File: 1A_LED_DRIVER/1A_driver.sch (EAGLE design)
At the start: 1 part

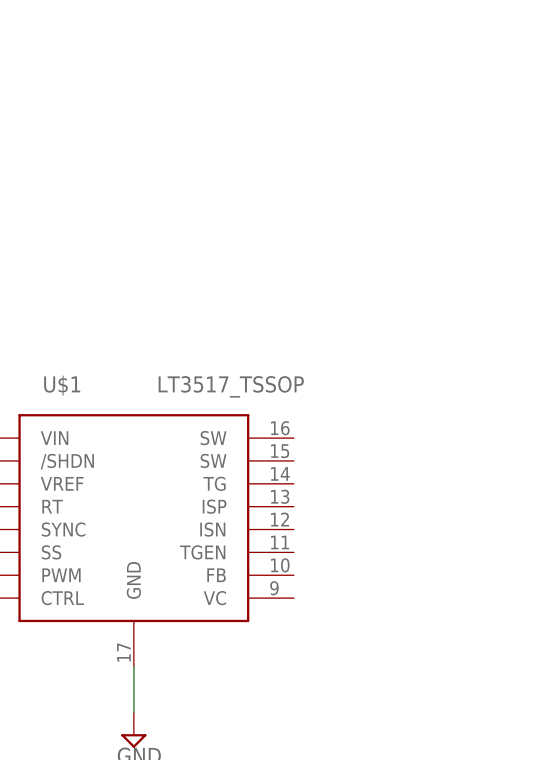
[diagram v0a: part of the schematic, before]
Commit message: making new mosfet lib
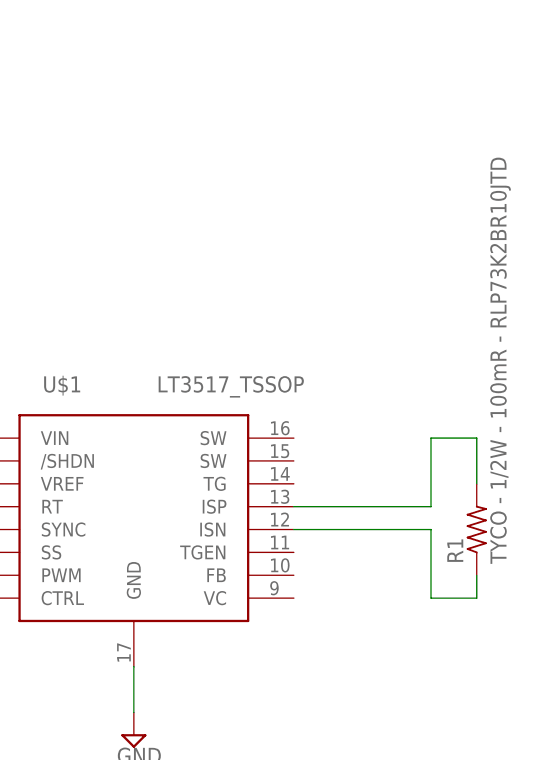
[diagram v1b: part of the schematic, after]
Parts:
- added R1: TYCO - 1/2W - 100mR - RLP73K2BR10JTD, standard_passive:RES_1206
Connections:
- new net N$1: R1.2, U$1.ISP@13
- new net N$2: R1.1, U$1.ISN@12
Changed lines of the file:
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@@
 <setting verticaltext="up"/>
 </settings>
-<grid distance="0.1" unitdist="inch" unit="inch" style="lines" multiple="1" display="yes" altdistance="0.01" altunitdist="inch" altunit="inch"/>
+<grid distance="0.1" unitdist="inch" unit="mm" style="lines" multiple="1" display="yes" altdistance="0.01" altunitdist="inch" altunit="mm"/>
 <layers>
 <layer number="1" name="Top" color="4" fill="1" visible="no" active="no"/>
@@
 <part name="U$1" library="LT3517" deviceset="LT3517_TSSOP" device=""/>
 <part name="SUPPLY1" library="supply2" deviceset="GND" device=""/>
+<part name="R1" library="standard_passive" deviceset="RES_1206" device="" value="TYCO - 1/2W - 100mR - RLP73K2BR10JTD"/>
 </parts>
 <sheets>
@@
 <instance part="U$1" gate="G$1" x="195.58" y="129.54"/>
 <instance part="SUPPLY1" gate="GND" x="195.58" y="104.14"/>
+<instance part="R1" gate="G$1" x="233.68" y="127" rot="R90"/>
 </instances>
 <busses>
@@
 </segment>
 </net>
+<net name="N$1" class="0">
+<segment>
+<pinref part="U$1" gate="G$1" pin="ISP@13"/>
+<wire x1="213.36" y1="129.54" x2="228.6" y2="129.54" width="0.1524" layer="91"/>
+<wire x1="228.6" y1="129.54" x2="228.6" y2="137.16" width="0.1524" layer="91"/>
+<wire x1="228.6" y1="137.16" x2="233.68" y2="137.16" width="0.1524" layer="91"/>
+<pinref part="R1" gate="G$1" pin="2"/>
+<wire x1="233.68" y1="137.16" x2="233.68" y2="132.08" width="0.1524" layer="91"/>
+</segment>
+</net>
+<net name="N$2" class="0">
+<segment>
+<pinref part="U$1" gate="G$1" pin="ISN@12"/>
+<wire x1="213.36" y1="127" x2="228.6" y2="127" width="0.1524" layer="91"/>
+<wire x1="228.6" y1="127" x2="228.6" y2="119.38" width="0.1524" layer="91"/>
+<wire x1="228.6" y1="119.38" x2="233.68" y2="119.38" width="0.1524" layer="91"/>
+<pinref part="R1" gate="G$1" pin="1"/>
+<wire x1="233.68" y1="119.38" x2="233.68" y2="121.92" width="0.1524" layer="91"/>
+</segment>
+</net>

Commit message: schematic finished
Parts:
- added C1, C2: 0.1u, standard_passive:CAP_0603
- added C3: 4.7u, standard_passive:CAP_1206
- added C4: 0.22u, standard_passive:CAP_0603
- added D1: RB060MM-60TF, DIODES:SCH_DIODE
- added L1: 6.8u, WE-PD:WE-PD-744771006_1260/1245/1280/1210
- added Q1: ZXMP6A13FTA, MOSFET:P-CHAN_MOSFET
- added R2, R3, R4, R5: (no value), standard_passive:RES_0603
- added R6: 6.04k, standard_passive:RES_0603
- added SV1: (no value), con-lstb:MA04-1
- added X1: 22-23-2021, con-molex:22-23-2021
- R1: value TYCO - 1/2W - 100mR - RLP73K2BR10JTD -> 100mR - 1/2W
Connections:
- new net N$10: C1.1, U$1.VC@9
- new net N$11: R6.1, U$1.RT@4
- new net N$3: Q1.G, U$1.TG@14
- new net N$4: D1.A, L1.2, U$1.SW@15, U$1.SW@16
- new net N$5: Q1.D, X1-1.S
- new net N$6: R2.1, R3.2, U$1.FB@10
- new net N$8: C2.2, U$1.SS@6
- new net N$9: R4.2, R5.1, U$1.CTRL@8
- new net PWM: SV1.3, U$1.PWM@7
- new net VIN: C3.1, L1.1, SV1.4, U$1./SHDN@2, U$1.VIN@1, X1-2.S
- new net VREF: R4.1, U$1.TGEN@11, U$1.VREF@3
- net GND: now also C1.2, C2.1, C4.2, R3.1, R5.2, R6.2, SV1.1, SV1.2, U$1.SYNC@5
- net N$1: now also C3.2, C4.1, D1.C, R2.2
- net N$2: now also Q1.S
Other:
- note added: "Only R4 if CTRL is not used"
- moved on the sheet: R1

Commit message: need to finish layout for the 1A regulator
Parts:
- added C5: 4.7u, standard_passive:CAP_1206
- added C7: 100u, rcl:CPOL-EUE5-5
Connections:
- net N$1 renamed I_P
- net N$2 renamed I_N
- net N$5 renamed I_LED
- net GND: now also C5.1, C7.-
- net VIN: now also C5.2, C7.+
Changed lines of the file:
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@@
 <setting verticaltext="up"/>
 </settings>
-<grid distance="0.1" unitdist="inch" unit="inch" style="lines" multiple="1" display="yes" altdistance="0.01" altunitdist="inch" altunit="inch"/>
+<grid distance="0.1" unitdist="inch" unit="mm" style="lines" multiple="1" display="yes" altdistance="0.01" altunitdist="inch" altunit="mm"/>
 <layers>
 <layer number="1" name="Top" color="4" fill="1" visible="no" active="no"/>
@@
 <part name="SV1" library="con-lstb" deviceset="MA04-1" device=""/>
 <part name="SUPPLY7" library="supply2" deviceset="GND" device=""/>
+<part name="C5" library="standard_passive" deviceset="CAP_1206" device="" value="4.7u"/>
+<part name="SUPPLY8" library="supply2" deviceset="GND" device=""/>
+<part name="C7" library="rcl" deviceset="CPOL-EU" device="E5-5" value="100u"/>
+<part name="SUPPLY9" library="supply2" deviceset="GND" device=""/>
 </parts>
 <sheets>
@@
 <instance part="SV1" gate="1" x="129.54" y="165.1"/>
 <instance part="SUPPLY7" gate="GND" x="142.24" y="152.4"/>
+<instance part="C5" gate="G$1" x="160.02" y="160.02" rot="R180"/>
+<instance part="SUPPLY8" gate="GND" x="160.02" y="152.4"/>
+<instance part="C7" gate="G$1" x="165.1" y="162.56"/>
+<instance part="SUPPLY9" gate="GND" x="165.1" y="152.4"/>
 </instances>
 <busses>
@@
 <junction x="142.24" y="160.02"/>
 </segment>
-</net>
-<net name="N$1" class="0">
+<segment>
+<pinref part="C5" gate="G$1" pin="1"/>
+<pinref part="SUPPLY8" gate="GND" pin="GND"/>
+<wire x1="160.02" y1="157.48" x2="160.02" y2="154.94" width="0.1524" layer="91"/>
+</segment>
+<segment>
+<pinref part="C7" gate="G$1" pin="-"/>
+<pinref part="SUPPLY9" gate="GND" pin="GND"/>
+<wire x1="165.1" y1="157.48" x2="165.1" y2="154.94" width="0.1524" layer="91"/>
+</segment>
+</net>
+<net name="I_P" class="0">
 <segment>
 <pinref part="U$1" gate="G$1" pin="ISP@13"/>
@@
 <wire x1="266.7" y1="160.02" x2="259.08" y2="160.02" width="0.1524" layer="91"/>
 <junction x="259.08" y="160.02"/>
-</segment>
-</net>
-<net name="N$2" class="0">
+<label x="223.52" y="129.54" size="1.778" layer="95"/>
+</segment>
+</net>
+<net name="I_N" class="0">
 <segment>
 <pinref part="U$1" gate="G$1" pin="ISN@12"/>
@@
 <wire x1="259.08" y1="119.38" x2="259.08" y2="114.3" width="0.1524" layer="91"/>
 <junction x="259.08" y="119.38"/>
+<label x="223.52" y="127" size="1.778" layer="95"/>
 </segment>
 </net>
@@
 </segment>
 </net>
-<net name="N$5" class="0">
+<net name="I_LED" class="0">
 <segment>
 <pinref part="Q1" gate="G$1" pin="D"/>
@@
 <pinref part="X1" gate="-1" pin="S"/>
 <wire x1="259.08" y1="99.06" x2="266.7" y2="99.06" width="0.1524" layer="91"/>
+<label x="261.62" y="99.06" size="1.778" layer="95"/>
 </segment>
 </net>
@@
 </net>
 <net name="VIN" class="0">
+<segment>
+<pinref part="X1" gate="-2" pin="S"/>
+<wire x1="266.7" y1="96.52" x2="248.92" y2="96.52" width="0.1524" layer="91"/>
+<label x="251.46" y="96.52" size="1.778" layer="95"/>
+</segment>
 <segment>
 <pinref part="L1" gate="G$1" pin="1"/>
@@
 <pinref part="C3" gate="G$1" pin="1"/>
 <wire x1="203.2" y1="160.02" x2="228.6" y2="160.02" width="0.1524" layer="91"/>
-</segment>
-<segment>
-<pinref part="X1" gate="-2" pin="S"/>
-<wire x1="266.7" y1="96.52" x2="248.92" y2="96.52" width="0.1524" layer="91"/>
-<label x="251.46" y="96.52" size="1.778" layer="95"/>
-</segment>
-<segment>
+<wire x1="172.72" y1="167.64" x2="172.72" y2="149.86" width="0.1524" layer="91"/>
+<junction x="172.72" y="149.86"/>
 <pinref part="SV1" gate="1" pin="4"/>
-<wire x1="137.16" y1="167.64" x2="149.86" y2="167.64" width="0.1524" layer="91"/>
-<label x="142.24" y="167.64" size="1.778" layer="95"/>
-</segment>
-</net>
+<wire x1="137.16" y1="167.64" x2="160.02" y2="167.64" width="0.1524" layer="91"/>
+<pinref part="C5" gate="G$1" pin="2"/>
+<wire x1="160.02" y1="167.64" x2="165.1" y2="167.64" width="0.1524" layer="91"/>
+<wire x1="165.1" y1="167.64" x2="172.72" y2="167.64" width="0.1524" layer="91"/>
+<wire x1="160.02" y1="165.1" x2="160.02" y2="167.64" width="0.1524" layer="91"/>
+<junction x="160.02" y="167.64"/>
+<pinref part="C7" gate="G$1" pin="+"/>
+<wire x1="165.1" y1="165.1" x2="165.1" y2="167.64" width="0.1524" layer="91"/>
+<junction x="165.1" y="167.64"/>
+</segment>
+</net>
